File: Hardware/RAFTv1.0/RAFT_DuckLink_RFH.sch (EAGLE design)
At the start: 130 parts, among them J1 AMPHENOL_132134, J2 AMPHENOL_132134, J4 Micro-USB, J5 132134-15, Q1 SIA817EDJ, Q2 SI7288DP, Q3 2N7002, U1 SX1276, U10 PE4259, U2 MAX2771ETI+, U3 ESP32-D0WD, U4 W25Q16BVSSIG, U5 INTERFACE-CP2102-GMR(QFN28), U6 PE4259, U7 SP0503BAHT, U8 BQ24650RVAR, U9 TPS63070RNMT, Y1 32.768kHz

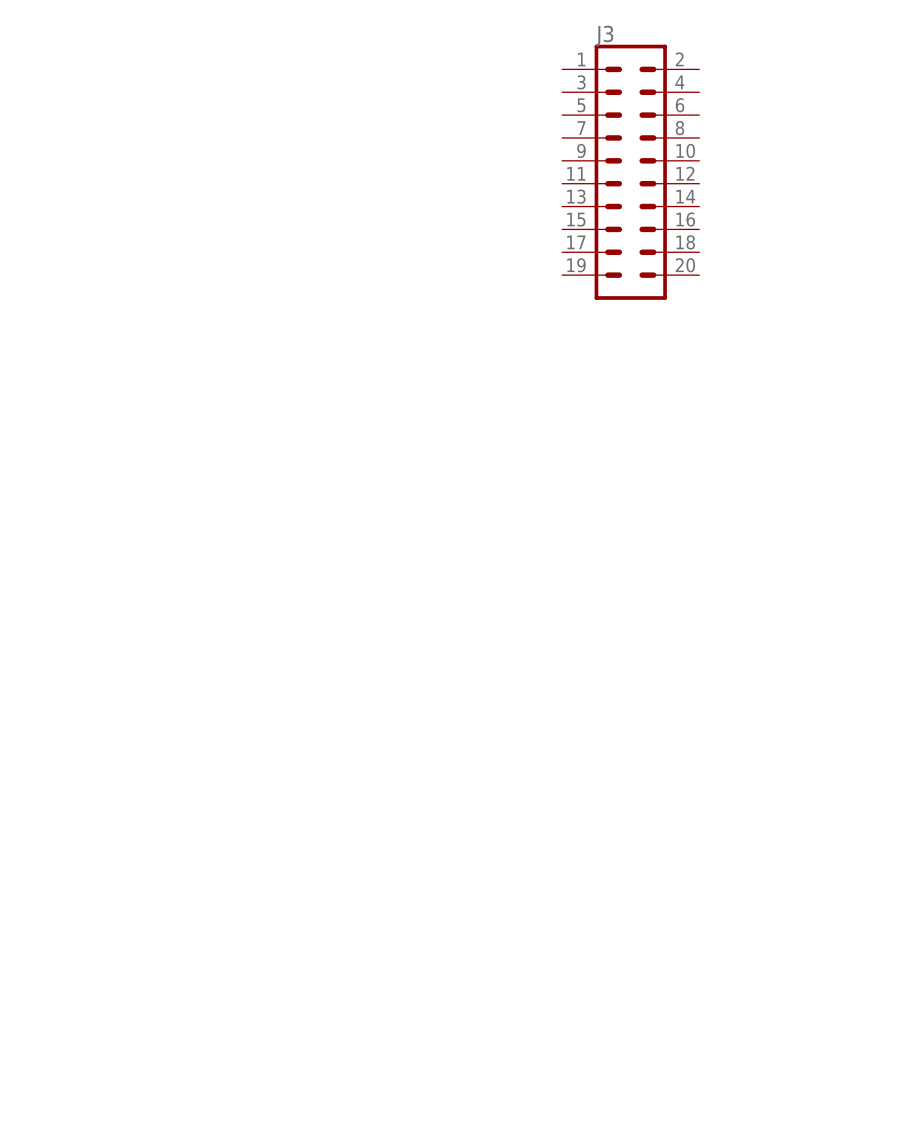
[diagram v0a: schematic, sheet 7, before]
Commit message: GPIO and rst switches for cpu/usb-uart
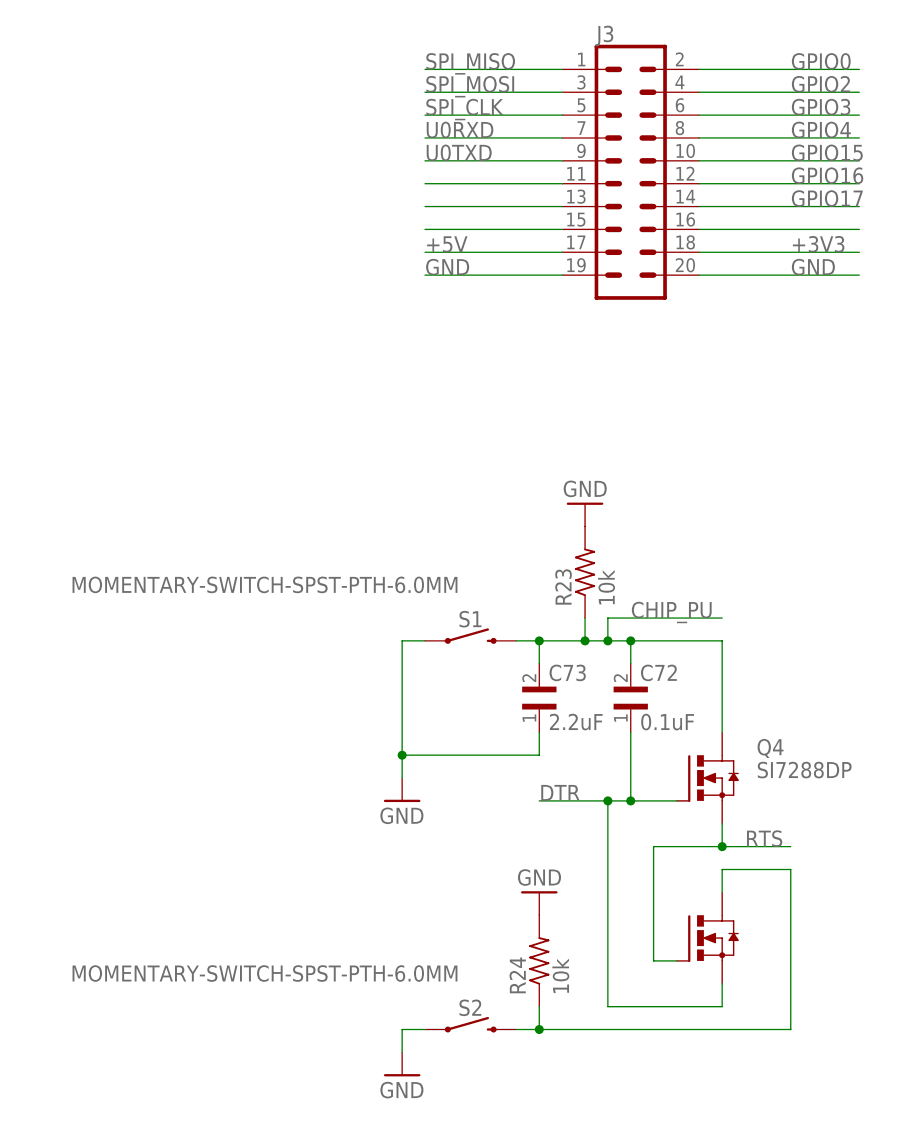
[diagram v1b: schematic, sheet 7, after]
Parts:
- added C72: 0.1uF, RAFT-components:GCM155R71C104KA55J
- added C73: 2.2uF, RAFT-components:GRM155D80J225ME95D
- added D5: PDS1040-13, PDS1040-13:PDS1040-13
- added Q4: SI7288DP, RAFT-components:SI7288DP
- added R23, R24: 10k, RAFT-components:CRCW040210K0JNED
- added S1, S2: MOMENTARY-SWITCH-SPST-PTH-6.0MM, SparkFun-Switches:MOMENTARY-SWITCH-SPST-PTH-6.0MM
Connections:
- net N$50 renamed ~RST
- removed net N$52: C54.2, C55.2, J4.VDD, U5.REGIN, U5.VBUS, U7.A
- removed net U0_DTR: U5.DTR
- removed net U0_RTS: U5.RTS
- new net +5V: C54.2, C55.2, D5.A, J3.17, J4.VDD, U5.REGIN, U5.VBUS, U7.A
- new net DTR: C72.1, Q4.G, Q4.S1, U5.DTR
- new net N$44: Q4.D1, R24.1, S2.2
- new net RTS: Q4.G1, Q4.S, U5.RTS
- new net SPI_MISO17: J3.16
- new net SPI_MISO5: J3.11
- new net SPI_MISO6: J3.13
- new net SPI_MISO7: J3.15
- net +3V3: now also J3.18
- net CHIP_PU: now also C72.2, C73.2, Q4.D, R23.1, S1.2
- net GND: now also C73.1, J3.19, J3.20, R23.2, R24.2, S1.1, S2.1, U5.GND
- net GPIO0: now also J3.2
- net GPIO15: now also J3.10
- net GPIO16: now also J3.12
- net GPIO17: now also J3.14
- net GPIO2: now also J3.4
- net GPIO3: now also J3.6
- net GPIO4: now also J3.8
- net SPI_CLK: now also J3.5
- net SPI_MISO: now also J3.1
- net SPI_MOSI: now also J3.3
- net U0RXD: now also J3.7
- net U0TXD: now also J3.9
- net VIN: now also D5.K
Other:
- moved on the sheet: R8

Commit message: typo/final edits
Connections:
- net ~RST renamed !RST
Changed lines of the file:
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@@
 </segment>
 </net>
-<net name="~RST" class="0">
+<net name="!RST" class="0">
 <segment>
 <pinref part="U5" gate="G$1" pin="!RST"/>

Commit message: PDF schematics
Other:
- note added: "GPIO/Hardware RST Swtchs."
- moved on the sheet: C72, C73, J3, Q4, R23, R24, S1, S2

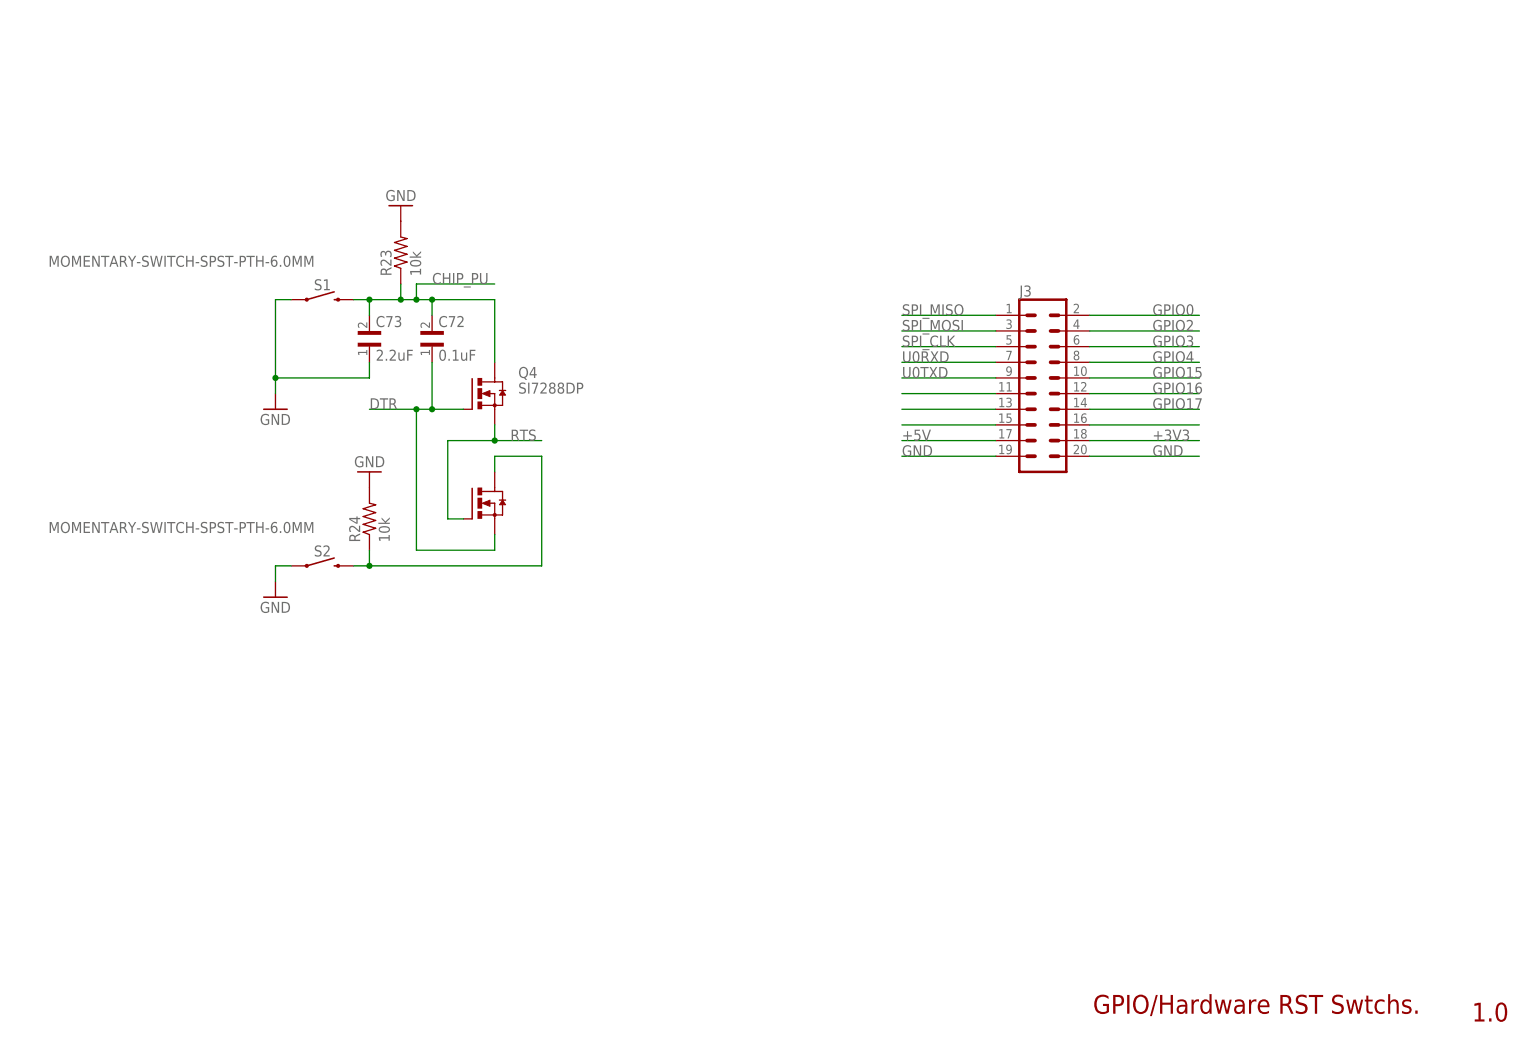
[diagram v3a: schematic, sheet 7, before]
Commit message: added internal antenna
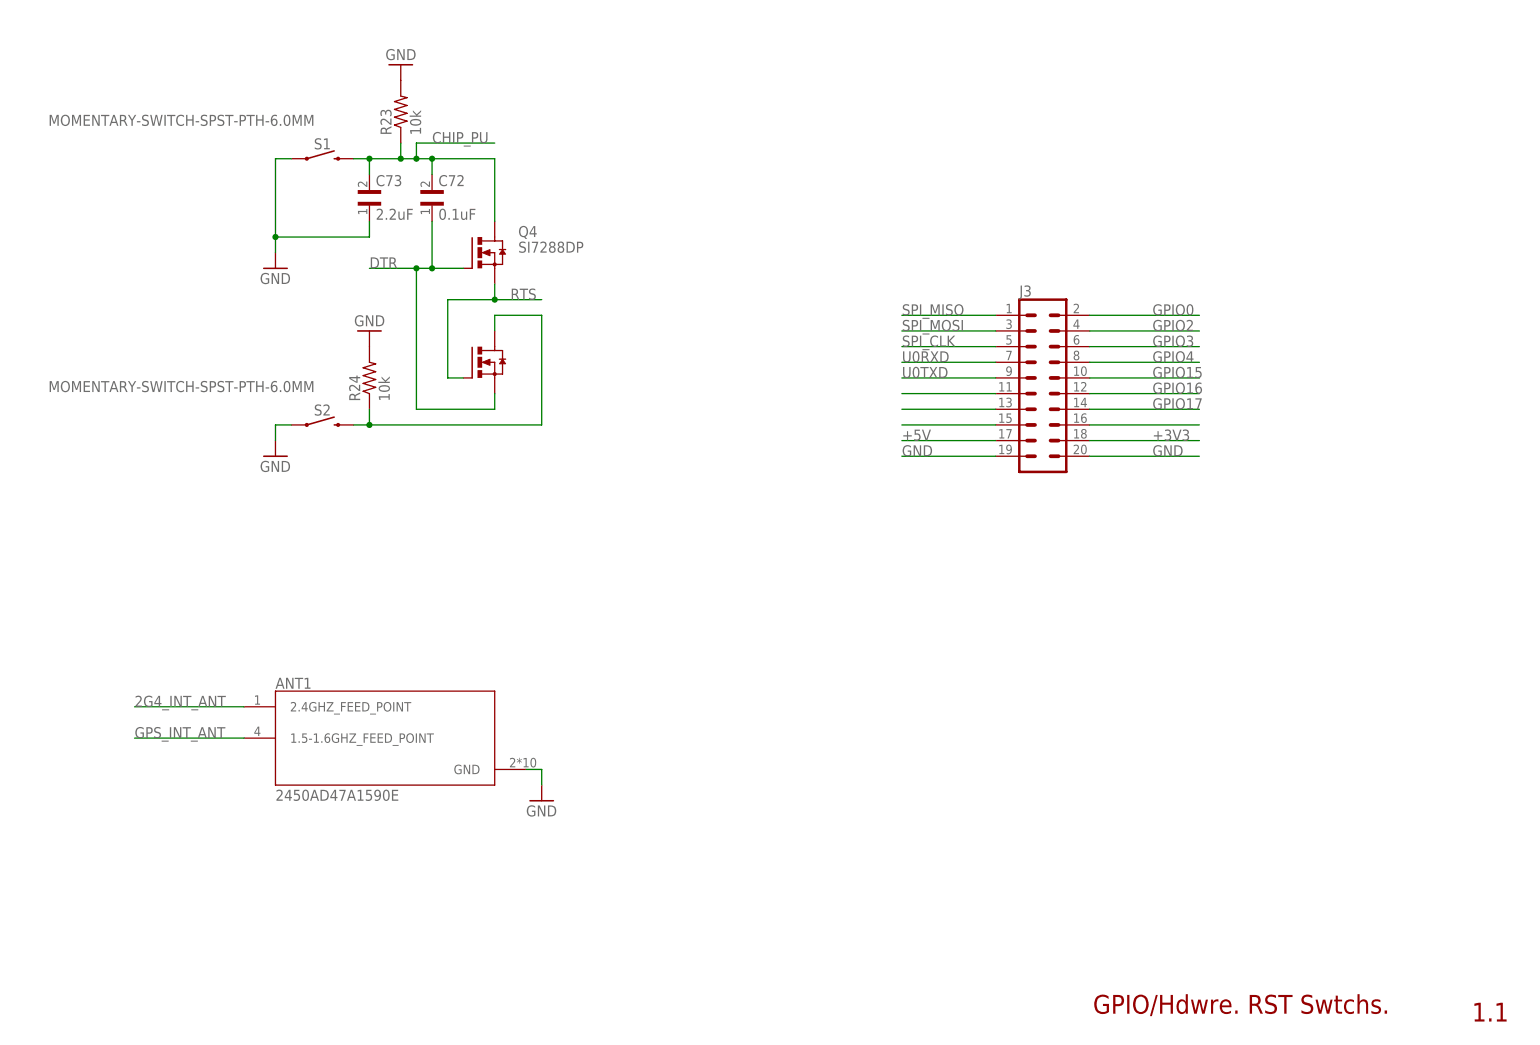
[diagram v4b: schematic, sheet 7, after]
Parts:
- added ANT1: 2450AD47A1590E, RAFT-components:2450AD47A1590E
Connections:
- net SPI_MISO17 renamed NC_4
- net SPI_MISO5 renamed NC_0
- net SPI_MISO6 renamed NC_1
- net SPI_MISO7 renamed NC_2
- net 2G4_INT_ANT: now also ANT1.2.4GHZ_FEED_POINT
- net GND: now also ANT1.GND
- net GPS_INT_ANT: now also ANT1.1.5-1.6GHZ_FEED_POINT
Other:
- note added: "GPIO/Hdwre. RST Swtchs."
- note removed: "GPIO/Hardware RST Swtchs."
- moved on the sheet: C72, C73, Q4, R23, R24, S1, S2

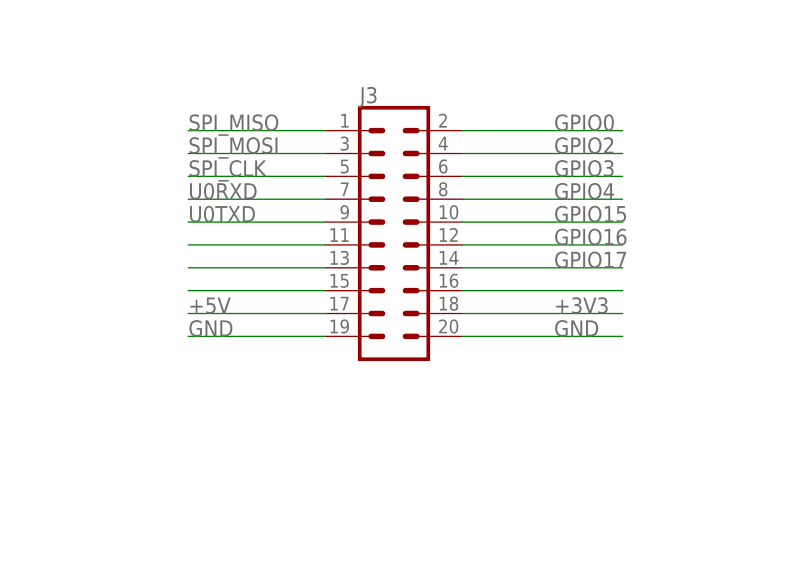
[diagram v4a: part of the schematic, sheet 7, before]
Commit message: added second 3V3 and 5V gpio header rails
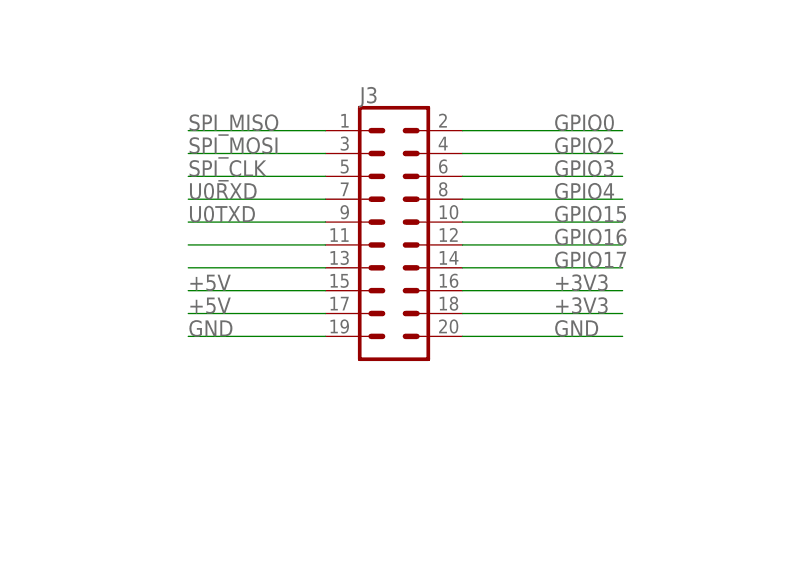
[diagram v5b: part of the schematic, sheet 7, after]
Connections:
- removed net NC_2: J3.15
- removed net NC_4: J3.16
- net +3V3: now also J3.16
- net +5V: now also J3.15
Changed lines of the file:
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@@
-</segment>
-</net>
-<net name="NC_2" class="0">
-<segment>
-<wire x1="55.88" y1="-27.94" x2="40.64" y2="-27.94" width="0.1524" layer="91"/>
-<pinref part="J3" gate="G$1" pin="15"/>
 </segment>
 </net>
@@
 <pinref part="J3" gate="G$1" pin="17"/>
 <label x="40.64" y="-30.48" size="1.778" layer="95"/>
+</segment>
+<segment>
+<wire x1="55.88" y1="-27.94" x2="40.64" y2="-27.94" width="0.1524" layer="91"/>
+<pinref part="J3" gate="G$1" pin="15"/>
+<label x="40.64" y="-27.94" size="1.778" layer="95"/>
 </segment>
 </net>
@@
 </segment>
 </net>
-<net name="NC_4" class="0">
-<segment>
-<wire x1="88.9" y1="-27.94" x2="71.12" y2="-27.94" width="0.1524" layer="91"/>
-<pinref part="J3" gate="G$1" pin="16"/>
-</segment>
-</net>
 <net name="+3V3" class="0">
 <segment>
@@
 <label x="81.28" y="-30.48" size="1.778" layer="95"/>
 </segment>
+<segment>
+<wire x1="88.9" y1="-27.94" x2="71.12" y2="-27.94" width="0.1524" layer="91"/>
+<pinref part="J3" gate="G$1" pin="16"/>
+<label x="81.28" y="-27.94" size="1.778" layer="95"/>
+</segment>
 </net>

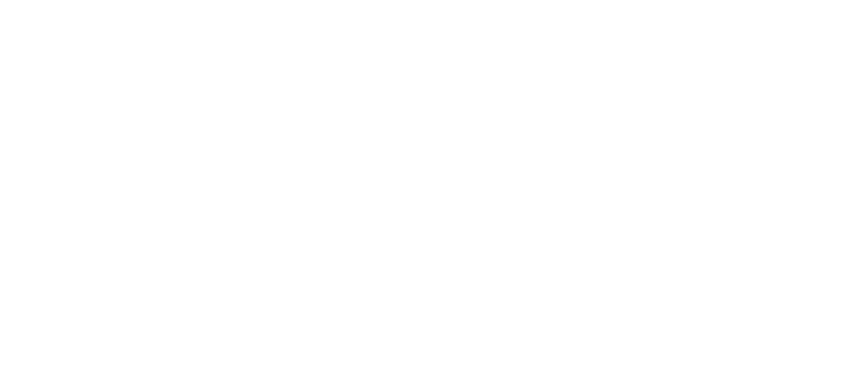
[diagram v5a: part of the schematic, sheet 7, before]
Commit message: Added 2-pin JST connector... again
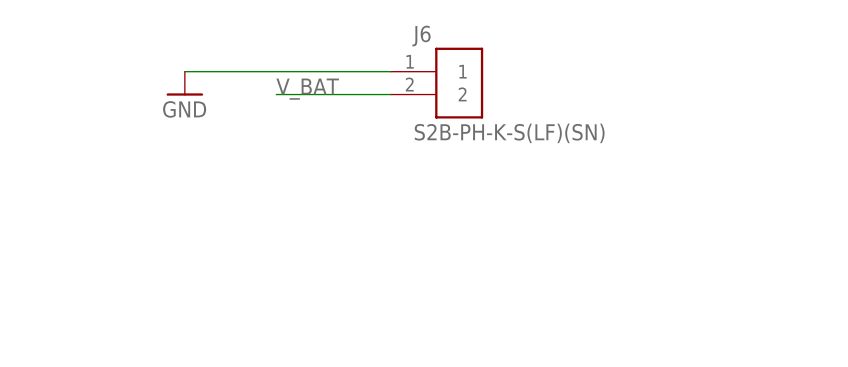
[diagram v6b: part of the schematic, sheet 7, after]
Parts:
- added J6: S2B-PH-K-S(LF)(SN), S2B-PH-K-S_LF__SN_:S2B-PH-K-S(LF)(SN)
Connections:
- removed net VOUT_BATT: C64.1, C65.2, C66.2, C67.2, Q1.D, R11.2, R_SR.2, U8.SRN
- new net V_BAT: C64.1, C65.2, C66.2, C67.2, J6.2, Q1.D, R11.2, R_SR.2, U8.SRN
- net GND: now also J6.1
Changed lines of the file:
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@@
 <part name="ANT1" library="RAFT-components" deviceset="2450AD47A1590E" device=""/>
 <part name="GND82" library="supply1" library_urn="urn:adsk.eagle:library:371" deviceset="GND" device=""/>
+<part name="J6" library="S2B-PH-K-S_LF__SN_" deviceset="S2B-PH-K-S(LF)(SN)" device=""/>
+<part name="GND83" library="supply1" library_urn="urn:adsk.eagle:library:371" deviceset="GND" device=""/>
 </parts>
 <sheets>
@@
 </segment>
 </net>
-<net name="VOUT_BATT" class="0">
-<segment>
-<pinref part="Q1" gate="G$1" pin="D"/>
-<wire x1="-88.9" y1="15.24" x2="-83.82" y2="15.24" width="0.1524" layer="91"/>
-<wire x1="-88.9" y1="15.24" x2="-88.9" y2="-2.54" width="0.1524" layer="91"/>
-<wire x1="-88.9" y1="-2.54" x2="-101.6" y2="-2.54" width="0.1524" layer="91"/>
-<label x="-104.14" y="-2.54" size="1.778" layer="95"/>
-</segment>
-</net>
 <net name="VIN" class="0">
 <segment>
@@
 </segment>
 </net>
+<net name="V_BAT" class="0">
+<segment>
+<pinref part="Q1" gate="G$1" pin="D"/>
+<wire x1="-88.9" y1="15.24" x2="-83.82" y2="15.24" width="0.1524" layer="91"/>
+<wire x1="-88.9" y1="15.24" x2="-88.9" y2="-2.54" width="0.1524" layer="91"/>
+<wire x1="-88.9" y1="-2.54" x2="-101.6" y2="-2.54" width="0.1524" layer="91"/>
+<label x="-104.14" y="-2.54" size="1.778" layer="95"/>
+</segment>
+</net>
 </nets>
 </sheet>
@@
 </segment>
 </net>
-<net name="VOUT_BATT" class="0">
+<net name="V_BAT" class="0">
 <segment>
 <wire x1="93.98" y1="-7.62" x2="93.98" y2="-2.54" width="0.1524" layer="91"/>
@@
 <attribute name="VALUE" x="-20.32" y="-91.44" size="1.778" layer="96"/>
 </instance>
+<instance part="J6" gate="G$1" x="60.96" y="33.02" smashed="yes">
+<attribute name="NAME" x="55.88" y="36.322" size="1.778" layer="95"/>
+<attribute name="VALUE" x="55.88" y="25.4" size="1.778" layer="96"/>
+</instance>
+<instance part="GND83" gate="1" x="30.48" y="30.48" smashed="yes">
+<attribute name="VALUE" x="27.94" y="27.94" size="1.778" layer="96"/>
+</instance>
 </instances>
 <busses>
@@
 <wire x1="-17.78" y1="-83.82" x2="-17.78" y2="-86.36" width="0.1524" layer="91"/>
 </segment>
+<segment>
+<pinref part="J6" gate="G$1" pin="1"/>
+<pinref part="GND83" gate="1" pin="GND"/>
+<wire x1="53.34" y1="33.02" x2="30.48" y2="33.02" width="0.1524" layer="91"/>
+</segment>
 </net>
 <net name="RTS" class="0">
@@
 </segment>
 </net>
+<net name="V_BAT" class="0">
+<segment>
+<pinref part="J6" gate="G$1" pin="2"/>
+<wire x1="53.34" y1="30.48" x2="40.64" y2="30.48" width="0.1524" layer="91"/>
+<label x="40.64" y="30.48" size="1.778" layer="95"/>
+</segment>
+</net>
